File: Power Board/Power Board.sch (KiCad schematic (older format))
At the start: 60 parts, among them J1 Conn_02x15_Counter_Clockwise, Q1 SI7135DP, Q2 SI7135DP, Q3 SI7135DP, Q4 SI7135DP, Q5 SI7135DP, Q6 SI7135DP, U1 LTC4417CGN, U2 TPS54308DDC, U3 TPS54308DDC, U4 TPS54308DDC

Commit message: Finished routing power board
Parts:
- removed C21: 22 uF, Capacitors_SMD:C_0805, symbol C_Small
- removed R14: 100 kΩ, Resistors_SMD:R_0603, symbol R_Small
- removed R15: 6.34 kΩ, Resistors_SMD:R_0603, symbol R_Small
- removed U4: TPS54308DDC, TO_SOT_Packages_SMD:SOT-23-6, symbol TPS54308DDC
- added C20: 15 uF, Capacitors_SMD:C_0805, symbol C_Small
- added C22: 1 uF, Capacitors_SMD:C_0603, symbol C_Small
- added C23: 4.7 uF, Capacitors_SMD:C_0603, symbol C_Small
- added U4: LTC3130-1, Housings_SSOP:MSOP-16-1EP_3x4mm_Pitch0.5mm, symbol LTC3130-1
- C18: value 0.1 uF -> 22nF; footprint Capacitors_SMD:C_0805 -> Capacitors_SMD:C_0603; Digikey Part Number 399-1171-1-ND -> 399-9043-1-ND
- C19: value 33 uF -> 22nF; footprint Capacitors_SMD:C_1206 -> Capacitors_SMD:C_0603; Digikey Part Number 445-8046-1-ND -> 399-9043-1-ND
- L3: value 16 uH -> 15 uH; footprint Inductors_SMD:L_Wuerth_HCI-1050 -> Custom Footprints:L_Wuerth_7447779115
- R1: value 93.1 kΩ -> 90.9 kΩ; Digikey Part Number 311-93.1KHRCT-ND -> 311-90.9KHRCT-ND
- R2: value 309 Ω -> 4.99 kΩ; Digikey Part Number 311-309HRCT-ND -> 311-4.99KHRCT-ND
- R3: value 5.36 kΩ -> 4.99 kΩ; Digikey Part Number 311-5.36KHRCT-ND -> 311-4.99KHRCT-ND
- R4, R7: value 93.1 kΩ -> 82.5 kΩ; Digikey Part Number 311-93.1KHRCT-ND -> 311-82.5KHRCT-ND
- R5, R8: value 2.49 kΩ -> 5.49 kΩ; Digikey Part Number 311-2.49KHRCT-ND -> 311-5.49KHRCT-ND
- R6, R9: value 5.9 kΩ -> 11 kΩ; Digikey Part Number 311-5.90KHRCT-ND -> 311-11.0KHRCT-ND
- renumbered C20 to C21, R16 to R14, R17 to R15, R18 to R16
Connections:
- wire segments 148 -> 140
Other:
- note added: "10-20 V"
- note added: "6-9 V"
- note removed: "12-17.1 V"
- note removed: "17.5-18.5 V"

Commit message: BOM Stuff
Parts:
- R16: Digikey Part Number none -> 311-100GRCT-ND
- U4: Digikey Part Number (none) -> LTC3130IMSE-1#PBF-ND
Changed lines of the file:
@@
 F 2 "Resistors_SMD:R_0603" V 2730 13900 50  0001 C CNN
 F 3 "" H 2800 13900 50  0001 C CNN
-F 4 "none" H 2880 14000 50  0001 C CNN "Digikey Part Number"
+F 4 "311-100GRCT-ND" H 2880 14000 50  0001 C CNN "Digikey Part Number"
 	1    2800 13900
 	0    1    1    0
@@
 F 2 "Housings_SSOP:MSOP-16-1EP_3x4mm_Pitch0.5mm" H 3200 11500 60  0001 C CNN
 F 3 "" H 3200 11500 60  0001 C CNN
+F 4 "LTC3130IMSE-1#PBF-ND" H 3200 11500 60  0001 C CNN "Digikey Part Number"
 	1    3200 11500
 	1    0    0    -1

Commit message: Updated power board to kicad 5
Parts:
- C1: symbol CP1_Small -> device:CP1_Small
- C10, C11, C12, C13, C14, C15, C16, C17, C18, C19, C2, C20, C21, C22, C23, C3, C4, C5, C6, C7, C8, C9: symbol C_Small -> device:C_Small
- D1, D3, D4: symbol D_TVS -> device:D_TVS
- D2: symbol D_Zener -> device:D_Zener
- D5, D6, D7: symbol LED -> device:LED
- J1: symbol Conn_02x15_Counter_Clockwise -> Power-Board-rescue:Conn_02x15_Counter_Clockwise
- L1, L2, L3: symbol L_Small -> device:L_Small
- Q1, Q2, Q3, Q4, Q5, Q6: symbol Q_PMOS_DGS -> device:Q_PMOS_DGS
- R1, R10, R11, R12, R13, R2, R3, R4, R5, R6, R7, R8, R9: symbol R_Small -> device:R_Small
- R14, R15, R16: symbol R -> device:R
- U1: symbol LTC4417CGN -> Custom-Parts:LTC4417CGN
- U2, U3: symbol TPS54308DDC -> Custom-Parts:TPS54308DDC
- U4: symbol LTC3130-1 -> Custom-Parts:LTC3130-1
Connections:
- wire segments 140 -> 196

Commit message: Forgot an openlog on the control board
Had to get rid of the fault detect pins on the TCs, will have to poll for faults over SPI now
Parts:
- R1: value 90.9 kΩ -> 82.5 kΩ; Digikey Part Number 311-90.9KHRCT-ND -> 311-82.5KHRCT-ND
- R2: value 4.99 kΩ -> 5.49 kΩ; Digikey Part Number 311-4.99KHRCT-ND -> 311-5.49KHRCT-ND
- R3: value 4.99 kΩ -> 11 kΩ; Digikey Part Number 311-4.99KHRCT-ND -> 311-11.0KHRCT-ND
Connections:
- net labels removed: +14V, SERVO1_VCC, SERVO2_VCC
- wire segments 196 -> 192
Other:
- note removed: "10-20 V"

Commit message: New Board shape
Thanks a lot James
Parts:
- removed C13: 0.1 uF, Capacitors_SMD:C_0805, symbol device:C_Small
- removed C14, C15: 15 uF, Capacitors_SMD:C_0805, symbol device:C_Small
- removed C16, C17: 22 uF, Capacitors_SMD:C_0805, symbol device:C_Small
- removed J1: Conn_02x15_Counter_Clockwise, Custom Footprints:CONN_CARD_02x15_MALE, symbol Power-Board-rescue:Conn_02x15_Counter_Clockwise
- removed L2: 18 uH, Inductors_SMD:L_Wuerth_HCI-1365, symbol device:L_Small
- removed R12: 100 kΩ, Resistors_SMD:R_0603, symbol device:R_Small
- removed R13: 22 kΩ, Resistors_SMD:R_0603, symbol device:R_Small
- removed U3: TPS54308DDC, TO_SOT_Packages_SMD:SOT-23-6, symbol Custom-Parts:TPS54308DDC
- added H1, H2, H3, H4: M3 Mounting Hole, Mounting_Holes:MountingHole_3.2mm_M3, symbol Mechanical:Mounting_Hole
- added J1, J2: Conn_02x25_Odd_Even, Pin_Headers:Pin_Header_Straight_2x25_Pitch1.27mm, symbol Connector:Conn_02x25_Odd_Even
- added SYM1: SYM_Arrow45_XLarge, Custom Parts:Logo_v3, symbol Graphic:SYM_Arrow45_XLarge
- renumbered C18 to C13, C19 to C14, C20 to C15, C21 to C16, C22 to C17, C23 to C18, L3 to L2, R14 to R12, R15 to R13, R16 to R14, U4 to U3
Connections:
- wire segments 192 -> 160

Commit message: A whole lot of changes
Kinda forgot what they all were
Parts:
- removed D1, D3, D4: SMBJ26CA, Diodes_SMD:D_SMB, symbol device:D_TVS
- removed D6: LED_R, LEDs:LED_0603, symbol device:LED
- removed J1, J2: Conn_02x25_Odd_Even, Pin_Headers:Pin_Header_Straight_2x25_Pitch1.27mm, symbol Connector:Conn_02x25_Odd_Even
- removed R13: 100 Ω, Resistors_SMD:R_0603, symbol device:R
- added J1: Conn_02x10_Odd_Even, Pin_Headers:Pin_Header_Straight_2x10_Pitch1.27mm, symbol Connector:Conn_02x10_Odd_Even
- added J2, J3, J4, J5: Conn_01x02, Custom Footprints:High_Current_Wires, symbol Connector:Conn_01x02
- renumbered D7 to D6, R14 to R13
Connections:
- wire segments 160 -> 148
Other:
- moved on the sheet: SYM1

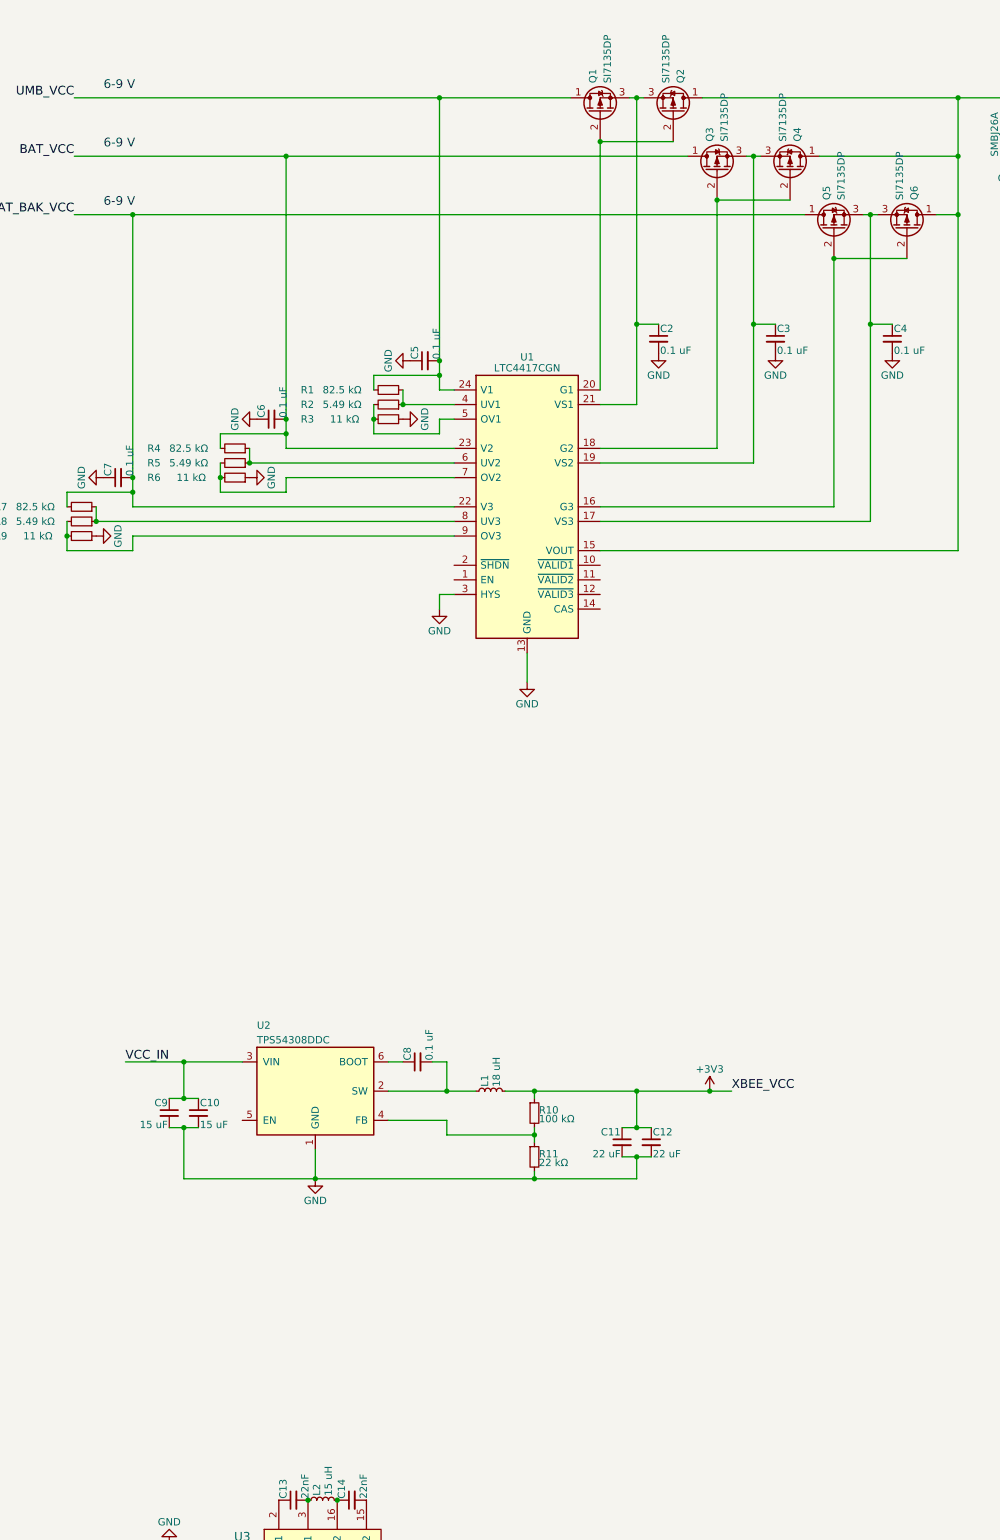
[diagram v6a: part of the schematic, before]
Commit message: Added comments and stuff for power board PCB review
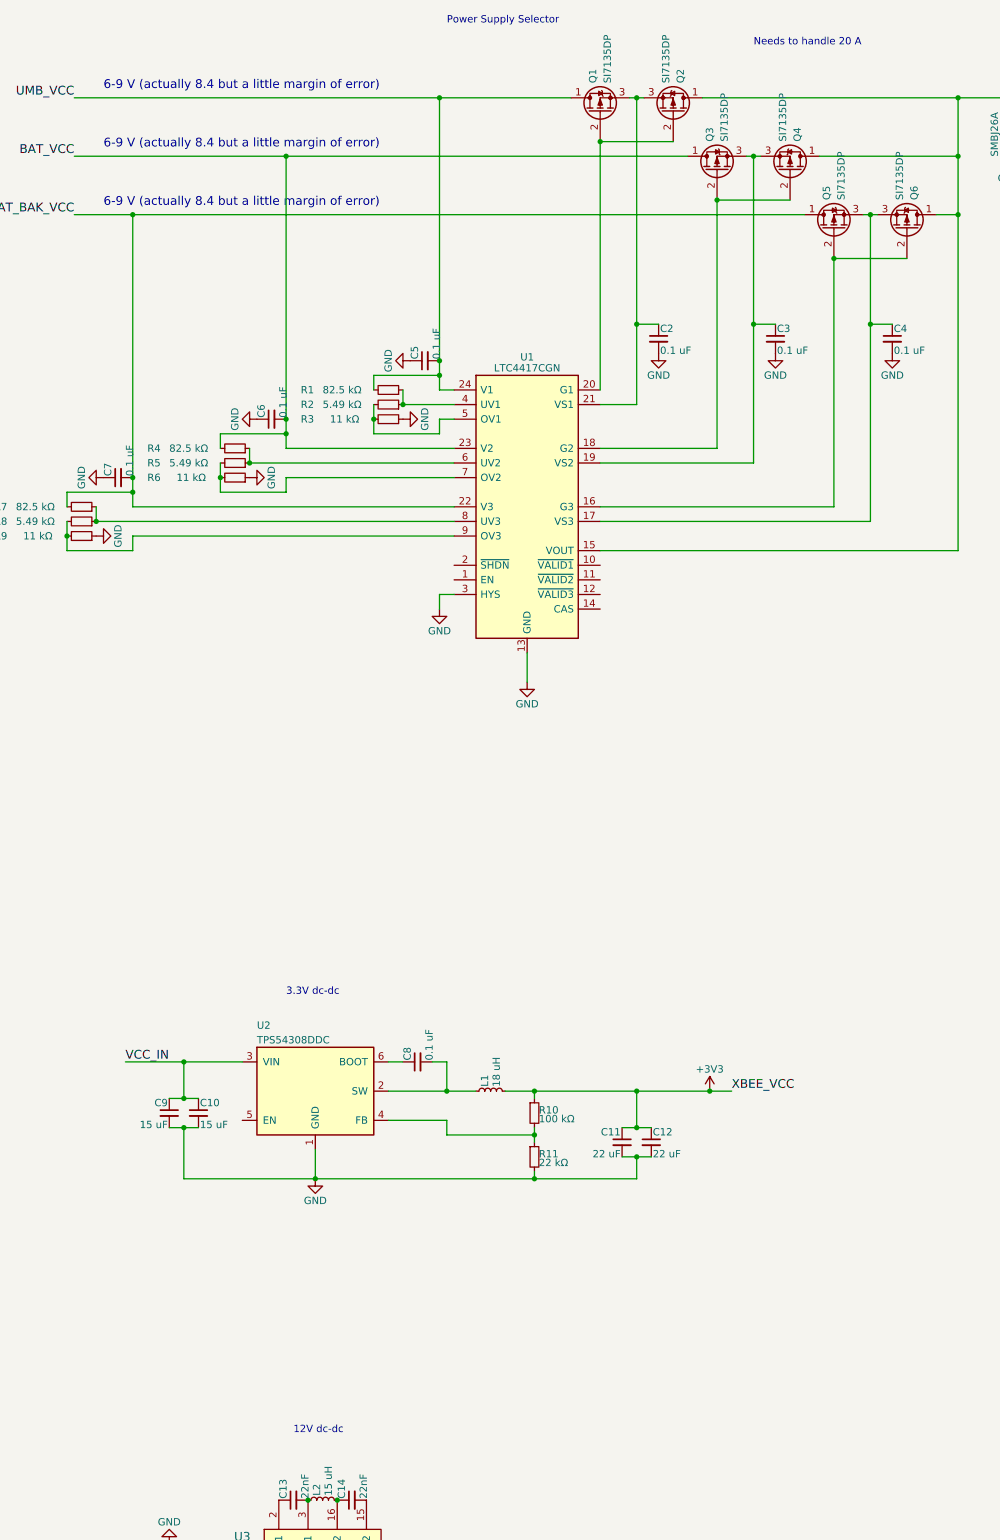
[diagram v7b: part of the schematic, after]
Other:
- note added: "12V dc-dc"
- note added: "3.3V dc-dc"
- note added: "6-9 V (actually 8.4 but a little margin of error)"
- note added: "Needs to handle 20 A"
- note added: "Power Supply Selector"
- note removed: "6-9 V"
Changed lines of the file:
@@
 VCC_IN
 Text Notes 1700 1050 0    60   ~ 0
-6-9 V
+6-9 V (actually 8.4 but a little margin of error)
 Text Notes 1700 1450 0    60   ~ 0
-6-9 V
+6-9 V (actually 8.4 but a little margin of error)
 Text Notes 1700 1850 0    60   ~ 0
-6-9 V
+6-9 V (actually 8.4 but a little margin of error)
 Text Label 1850 7700 0    60   ~ 0
 VCC_IN
@@
 Wire Wire Line
 	4000 1100 4900 1100
+Text Notes 6150 750  0    50   ~ 0
+Needs to handle 20 A
+Text Notes 2950 7250 0    50   ~ 0
+3.3V dc-dc
+Text Notes 3000 10250 0    50   ~ 0
+12V dc-dc
+Text Notes 4050 600  0    50   ~ 0
+Power Supply Selector
 $EndSCHEMATC

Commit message: a
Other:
- note added: "If this shows up as a box with a question mark\nlook at the exported pdf schematic instead"
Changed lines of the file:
@@
 encoding utf-8
 Sheet 1 1
-Title ""
-Date ""
-Rev ""
-Comp ""
+Title "Avionics Power Board"
+Date "2018-03-20"
+Rev "0.8"
+Comp "UAH SHC Spaceport America Cup"
 Comment1 ""
 Comment2 ""
@@
 Text Notes 4050 600  0    50   ~ 0
 Power Supply Selector
+Text Notes 4950 5050 0    50   ~ 0
+If this shows up as a box with a question mark\nlook at the exported pdf schematic instead
 $EndSCHEMATC
